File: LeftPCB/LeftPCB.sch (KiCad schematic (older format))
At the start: 1 part, among them J1 Bridge_Conn

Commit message: Updated schematic for LeftPCB, completed USB hub and Keyboard HID device, and started work on the power supply have the external, 3.3v, and 5v mapped out, just need to figure out battery charging/usage circuits.
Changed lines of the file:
@@
 $Descr A4 11693 8268
 encoding utf-8
-Sheet 1 2
+Sheet 1 3
 Title ""
 Date ""
@@
 	6350 1350 6150 1350
 $Sheet
-S 7750 1000 850  2650
+S 8050 1000 850  2650
 U 5F1B6B4F
 F0 "LeftPCB_PWR" 50

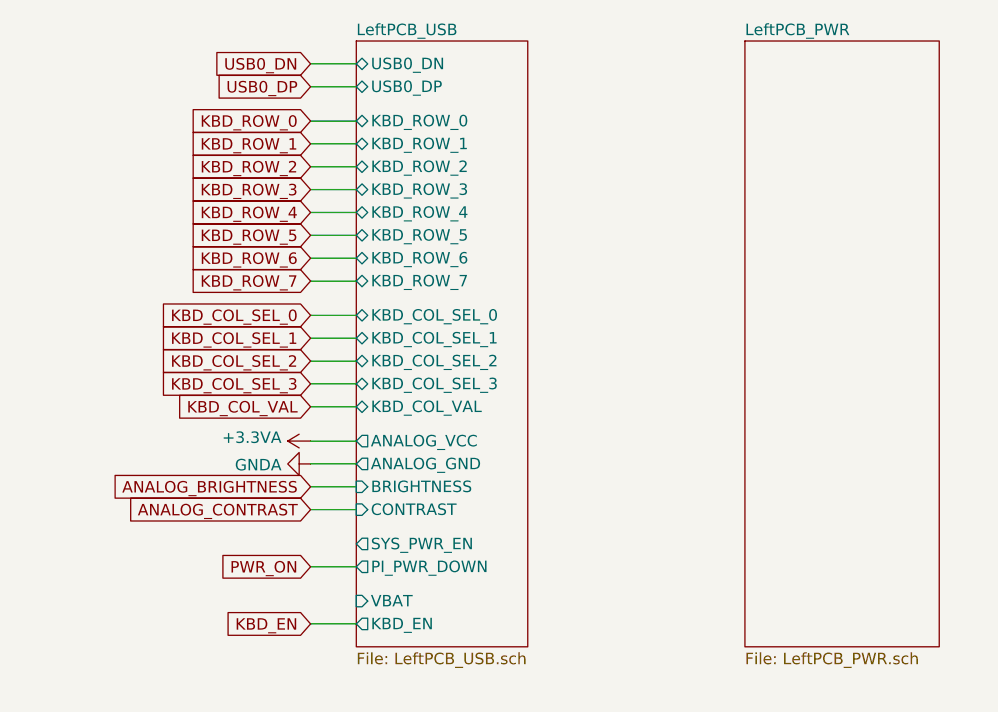
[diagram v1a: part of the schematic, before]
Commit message: Completed most of left side schematic and started working on layout.
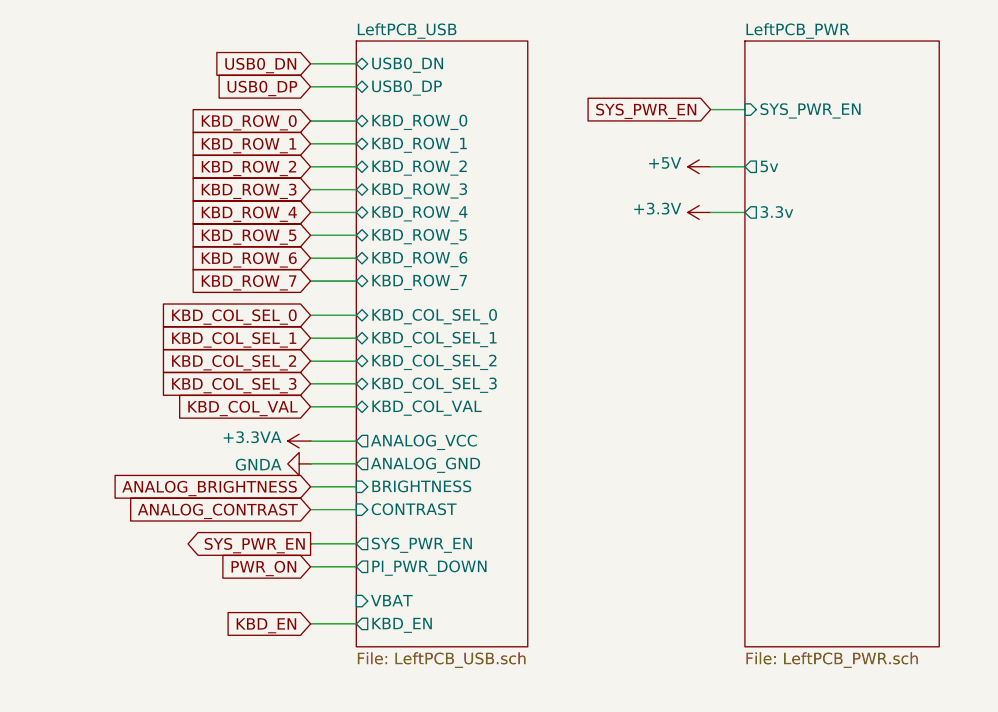
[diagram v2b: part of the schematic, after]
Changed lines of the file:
@@
 PWR_ON
 $Comp
-L power:GNDA #PWR?
+L power:GNDA #PWR0106
 U 1 1 5F18B947
 P 6150 2850
-F 0 "#PWR?" H 6150 2600 50  0001 C CNN
+F 0 "#PWR0106" H 6150 2600 50  0001 C CNN
 F 1 "GNDA" V 6155 2723 50  0000 R CNN
 F 2 "" H 6150 2850 50  0001 C CNN
@@
 $EndComp
 $Comp
-L power:+3.3VA #PWR?
+L power:+3.3VA #PWR0107
 U 1 1 5F18C4C7
 P 6150 2750
-F 0 "#PWR?" H 6150 2600 50  0001 C CNN
+F 0 "#PWR0107" H 6150 2600 50  0001 C CNN
 F 1 "+3.3VA" V 6165 2877 50  0000 L CNN
 F 2 "" H 6150 2750 50  0001 C CNN
@@
 F0 "LeftPCB_PWR" 50
 F1 "LeftPCB_PWR.sch" 50
+F2 "SYS_PWR_EN" I L 8050 1300 50
+F3 "5v" O L 8050 1550 50
+F4 "3.3v" O L 8050 1750 50
 $EndSheet
+$Comp
+L power:+3.3V #PWR0134
+U 1 1 5EE3518D
+P 7900 1750
+F 0 "#PWR0134" H 7900 1600 50  0001 C CNN
+F 1 "+3.3V" V 7915 1878 50  0000 L CNN
+F 2 "" H 7900 1750 50  0001 C CNN
+F 3 "" H 7900 1750 50  0001 C CNN
+	1    7900 1750
+	0    -1   -1   0
+$EndComp
+$Comp
+L power:+5V #PWR0135
+U 1 1 5EE35D6E
+P 7900 1550
+F 0 "#PWR0135" H 7900 1400 50  0001 C CNN
+F 1 "+5V" V 7915 1678 50  0000 L CNN
+F 2 "" H 7900 1550 50  0001 C CNN
+F 3 "" H 7900 1550 50  0001 C CNN
+	1    7900 1550
+	0    -1   -1   0
+$EndComp
+Text GLabel 6150 3200 0    50   Output ~ 0
+SYS_PWR_EN
+Wire Wire Line
+	6150 3200 6350 3200
+Text GLabel 7900 1300 0    50   Input ~ 0
+SYS_PWR_EN
+Wire Wire Line
+	7900 1300 8050 1300
+Wire Wire Line
+	8050 1550 7900 1550
+Wire Wire Line
+	7900 1750 8050 1750
 $EndSCHEMATC

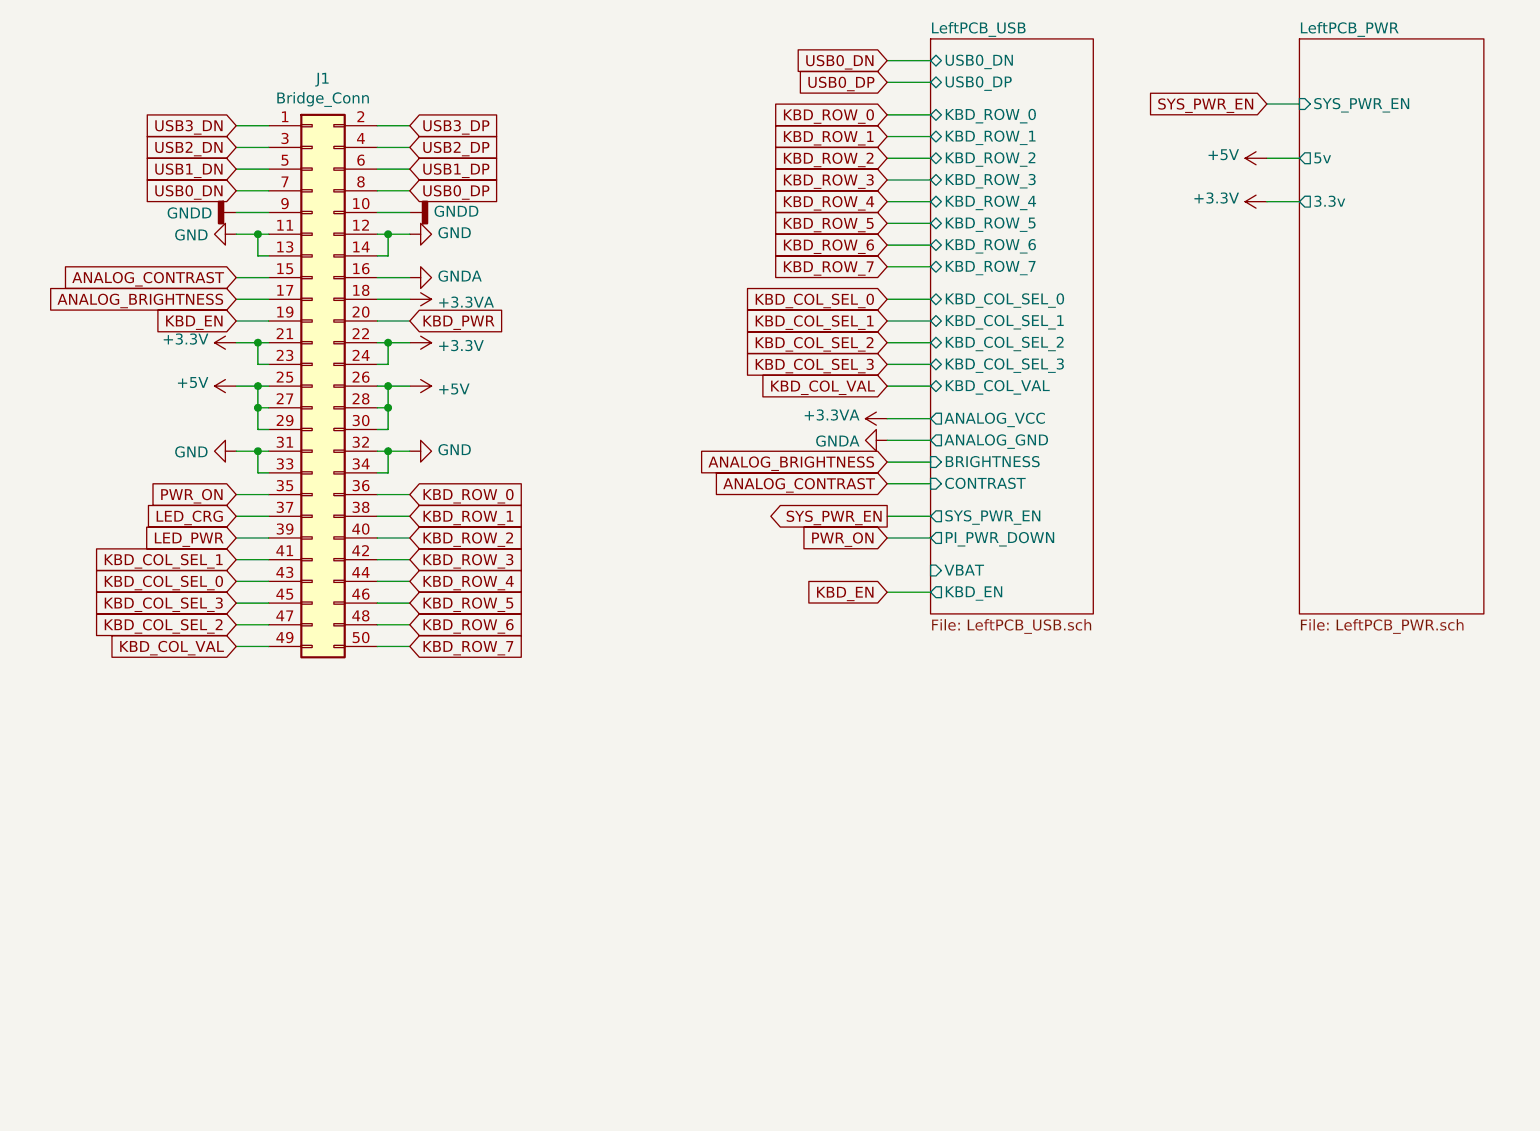
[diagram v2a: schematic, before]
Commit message: Updated and performed layout on most of left PCB, still have a few things to add.
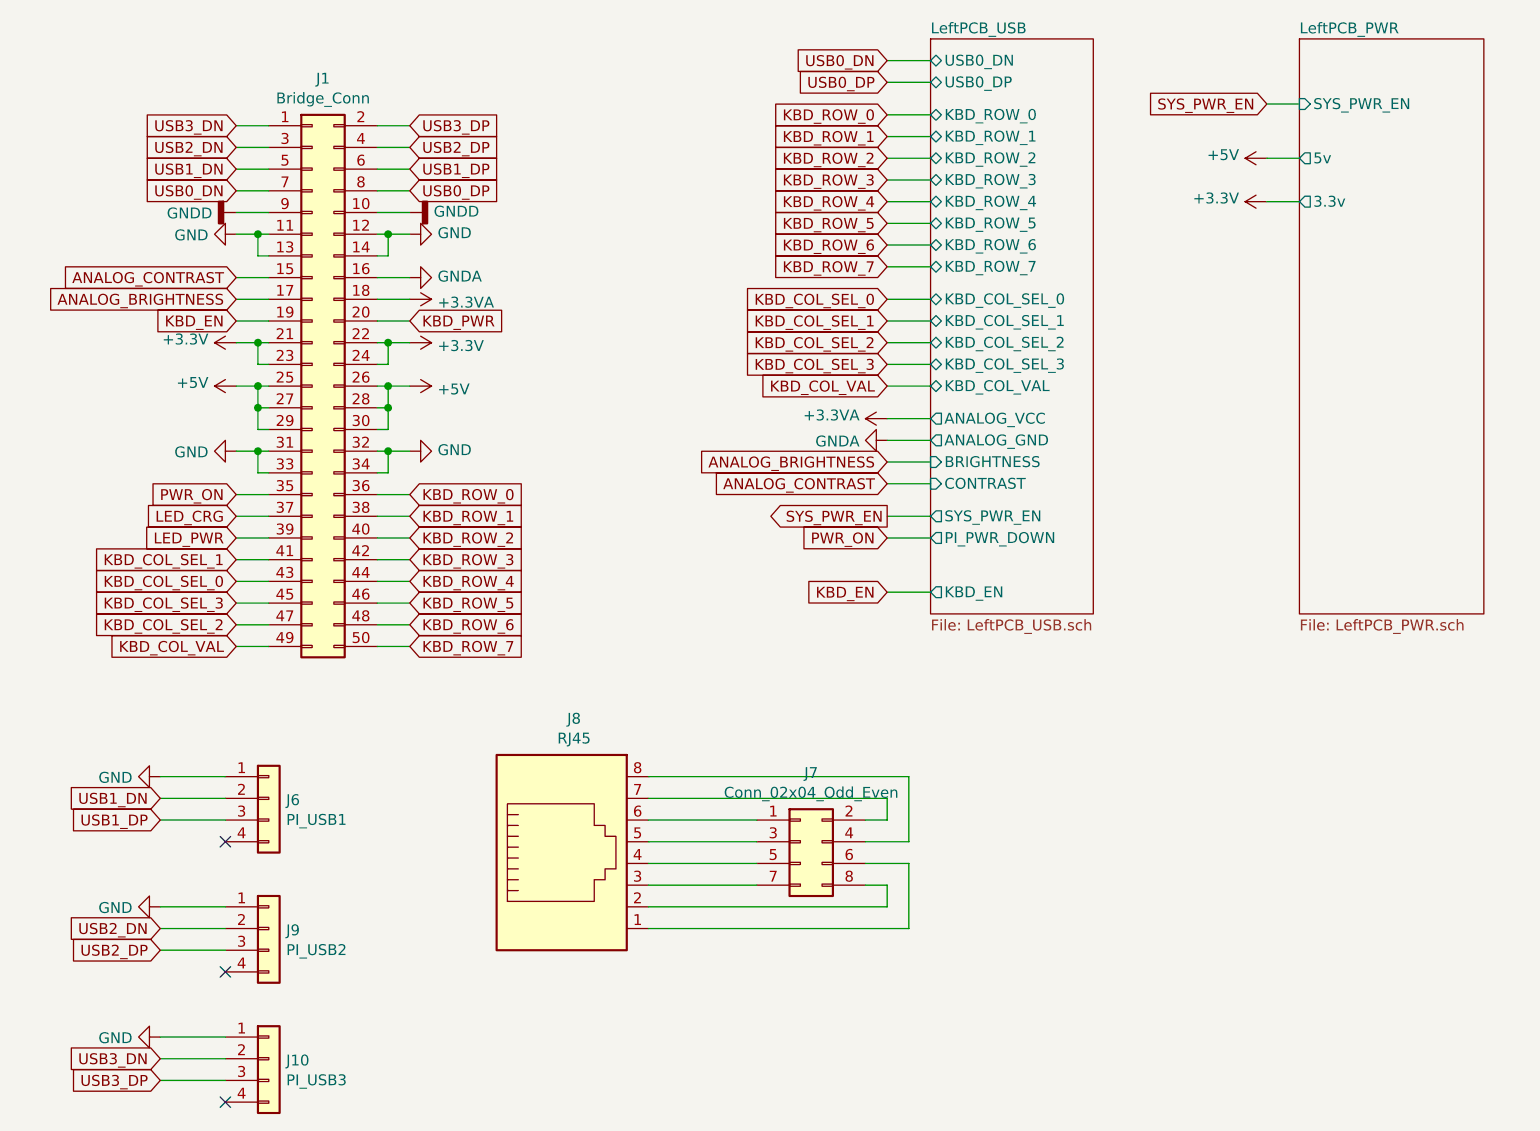
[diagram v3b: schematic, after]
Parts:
- added J10: PI_USB3, Pin_Headers:Pin_Header_Straight_1x04_Pitch1.00mm, symbol Connector_Generic:Conn_01x04
- added J6: PI_USB1, Pin_Headers:Pin_Header_Straight_1x04_Pitch1.00mm, symbol Connector_Generic:Conn_01x04
- added J7: Conn_02x04_Odd_Even, Pin_Headers:Pin_Header_Straight_2x04_Pitch1.00mm, symbol Connector_Generic:Conn_02x04_Odd_Even
- added J8: RJ45, Connectors:RJ45_8, symbol Connector:RJ45
- added J9: PI_USB2, Pin_Headers:Pin_Header_Straight_1x04_Pitch1.00mm, symbol Connector_Generic:Conn_01x04
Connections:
- net GND: now also J10.1 (Pin_1), J6.1 (Pin_1), J9.1 (Pin_1)
- net USB1_DN: now also J6.2 (Pin_2)
- net USB1_DP: now also J6.3 (Pin_3)
- net USB2_DN: now also J9.2 (Pin_2)
- net USB2_DP: now also J9.3 (Pin_3)
- net USB3_DN: now also J10.2 (Pin_2)
- net USB3_DP: now also J10.3 (Pin_3)
- new net: J7.6 (Pin_6), J8.1
- new net: J7.8 (Pin_8), J8.2
- new net: J7.7 (Pin_7), J8.3
- new net: J7.5 (Pin_5), J8.4
- new net: J7.3 (Pin_3), J8.5
- new net: J7.1 (Pin_1), J8.6
- new net: J7.2 (Pin_2), J8.7
- new net: J7.4 (Pin_4), J8.8
- no-connect marks 0 -> 3
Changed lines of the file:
@@
 F20 "CONTRAST" I L 6350 3050 50
 F21 "SYS_PWR_EN" O L 6350 3200 50
-F22 "VBAT" I L 6350 3450 50
-F23 "PI_PWR_DOWN" O L 6350 3300 50
-F24 "KBD_EN" O L 6350 3550 50
+F22 "PI_PWR_DOWN" O L 6350 3300 50
+F23 "KBD_EN" O L 6350 3550 50
 $EndSheet
 Text GLabel 6150 1200 0    50   Input ~ 0
@@
 Wire Wire Line
 	7900 1750 8050 1750
+$Comp
+L Connector_Generic:Conn_01x04 J6
+U 1 1 5F290991
+P 3300 4500
+F 0 "J6" H 3380 4492 50  0000 L CNN
+F 1 "PI_USB1" H 3380 4401 50  0000 L CNN
+F 2 "Pin_Headers:Pin_Header_Straight_1x04_Pitch1.00mm" H 3300 4500 50  0001 C CNN
+F 3 "~" H 3300 4500 50  0001 C CNN
+	1    3300 4500
+	1    0    0    -1
+$EndComp
+$Comp
+L Connector_Generic:Conn_01x04 J9
+U 1 1 5F291372
+P 3300 5100
+F 0 "J9" H 3380 5092 50  0000 L CNN
+F 1 "PI_USB2" H 3380 5001 50  0000 L CNN
+F 2 "Pin_Headers:Pin_Header_Straight_1x04_Pitch1.00mm" H 3300 5100 50  0001 C CNN
+F 3 "~" H 3300 5100 50  0001 C CNN
+	1    3300 5100
+	1    0    0    -1
+$EndComp
+$Comp
+L Connector_Generic:Conn_01x04 J10
+U 1 1 5F2924EB
+P 3300 5700
+F 0 "J10" H 3380 5692 50  0000 L CNN
+F 1 "PI_USB3" H 3380 5601 50  0000 L CNN
+F 2 "Pin_Headers:Pin_Header_Straight_1x04_Pitch1.00mm" H 3300 5700 50  0001 C CNN
+F 3 "~" H 3300 5700 50  0001 C CNN
+	1    3300 5700
+	1    0    0    -1
+$EndComp
+$Comp
+L power:GND #PWR045
+U 1 1 5F293EFF
+P 2800 4400
+F 0 "#PWR045" H 2800 4150 50  0001 C CNN
+F 1 "GND" V 2805 4272 50  0000 R CNN
+F 2 "" H 2800 4400 50  0001 C CNN
+F 3 "" H 2800 4400 50  0001 C CNN
+	1    2800 4400
+	0    1    1    0
+$EndComp
+$Comp
+L power:GND #PWR046
+U 1 1 5F29421B
+P 2800 5000
+F 0 "#PWR046" H 2800 4750 50  0001 C CNN
+F 1 "GND" V 2805 4872 50  0000 R CNN
+F 2 "" H 2800 5000 50  0001 C CNN
+F 3 "" H 2800 5000 50  0001 C CNN
+	1    2800 5000
+	0    1    1    0
+$EndComp
+$Comp
+L power:GND #PWR047
+U 1 1 5F294612
+P 2800 5600
+F 0 "#PWR047" H 2800 5350 50  0001 C CNN
+F 1 "GND" V 2805 5472 50  0000 R CNN
+F 2 "" H 2800 5600 50  0001 C CNN
+F 3 "" H 2800 5600 50  0001 C CNN
+	1    2800 5600
+	0    1    1    0
+$EndComp
+Text GLabel 2800 4500 0    50   Input ~ 0
+USB1_DN
+Text GLabel 2800 5100 0    50   Input ~ 0
+USB2_DN
+Text GLabel 2800 5700 0    50   Input ~ 0
+USB3_DN
+Text GLabel 2800 4600 0    50   Input ~ 0
+USB1_DP
+Text GLabel 2800 5200 0    50   Input ~ 0
+USB2_DP
+Text GLabel 2800 5800 0    50   Input ~ 0
+USB3_DP
+NoConn ~ 3100 4700
+NoConn ~ 3100 5300
+NoConn ~ 3100 5900
+Wire Wire Line
+	2800 4400 3100 4400
+Wire Wire Line
+	3100 4500 2800 4500
+Wire Wire Line
+	2800 4600 3100 4600
+Wire Wire Line
+	3100 5000 2800 5000
+Wire Wire Line
+	2800 5100 3100 5100
+Wire Wire Line
+	3100 5200 2800 5200
+Wire Wire Line
+	2800 5600 3100 5600
+Wire Wire Line
+	3100 5700 2800 5700
+Wire Wire Line
+	2800 5800 3100 5800
+$Comp
+L Connector:RJ45 J8
+U 1 1 5F2C0306
+P 4650 4800
+F 0 "J8" H 4707 5467 50  0000 C CNN
+F 1 "RJ45" H 4707 5376 50  0000 C CNN
+F 2 "Connectors:RJ45_8" V 4650 4825 50  0001 C CNN
+F 3 "~" V 4650 4825 50  0001 C CNN
+	1    4650 4800
+	1    0    0    -1
+$EndComp
+$Comp
+L Connector_Generic:Conn_02x04_Odd_Even J7
+U 1 1 5F2C29A6
+P 5750 4700
+F 0 "J7" H 5800 5017 50  0000 C CNN
+F 1 "Conn_02x04_Odd_Even" H 5800 4926 50  0000 C CNN
+F 2 "Pin_Headers:Pin_Header_Straight_2x04_Pitch1.00mm" H 5750 4700 50  0001 C CNN
+F 3 "~" H 5750 4700 50  0001 C CNN
+	1    5750 4700
+	1    0    0    -1
+$EndComp
+Wire Wire Line
+	5050 4600 5550 4600
+Wire Wire Line
+	5550 4700 5050 4700
+Wire Wire Line
+	5050 4800 5550 4800
+Wire Wire Line
+	5550 4900 5050 4900
+Wire Wire Line
+	5050 5000 6150 5000
+Wire Wire Line
+	6150 5000 6150 4900
+Wire Wire Line
+	6150 4900 6050 4900
+Wire Wire Line
+	5050 5100 6250 5100
+Wire Wire Line
+	6250 5100 6250 4800
+Wire Wire Line
+	6250 4800 6050 4800
+Wire Wire Line
+	5050 4500 6150 4500
+Wire Wire Line
+	6150 4500 6150 4600
+Wire Wire Line
+	6150 4600 6050 4600
+Wire Wire Line
+	5050 4400 6250 4400
+Wire Wire Line
+	6250 4400 6250 4700
+Wire Wire Line
+	6250 4700 6050 4700
 $EndSCHEMATC
